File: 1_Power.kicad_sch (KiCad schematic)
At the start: 35 parts, among them Q201 IRLZ44N, Q202 IRLZ44N, U201 BQ24005, U202 LM74700, U203 LM74700, U204 NCP1117-3.3, U205 LMR51430, U206 TPS7A2033PDBVR

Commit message: Changed oscillator series resistors to DNP
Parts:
- D201, D202: footprint (none) -> LED_SMD:LED_0603_1608Metric
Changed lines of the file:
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@@
 			)
 		)
-		(property "Footprint" ""
+		(property "Footprint" "LED_SMD:LED_0603_1608Metric"
 			(at 88.9 119.38 0)
 			(hide yes)
@@
 			)
 		)
-		(property "Footprint" ""
+		(property "Footprint" "LED_SMD:LED_0603_1608Metric"
 			(at 95.25 116.84 0)
 			(hide yes)

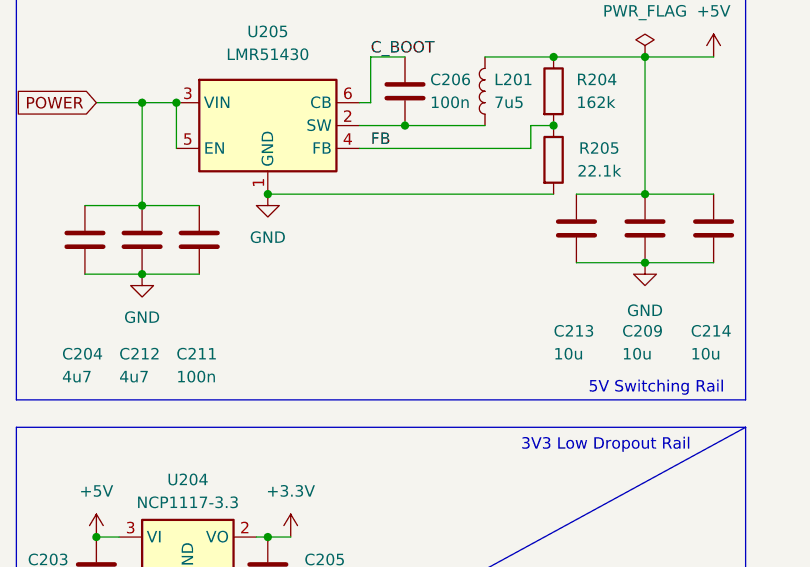
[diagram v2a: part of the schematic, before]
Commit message: Added switching regulator notes
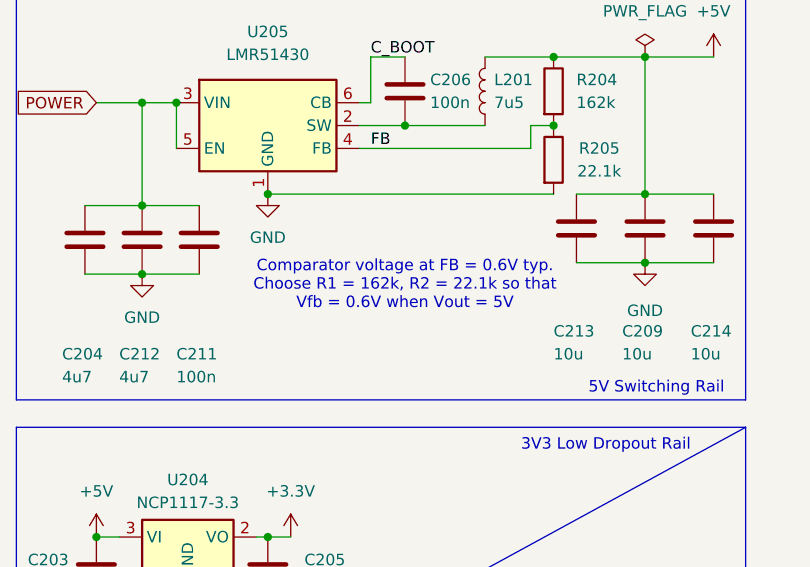
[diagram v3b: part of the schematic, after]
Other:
- note added: "Comparator voltage at FB = 0.6V typ. Choose R1 = 162k, R2 = 22.1k so that Vfb = 0.6V when Vout = 5V"
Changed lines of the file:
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@@
+		)
+	)
+	(text "Comparator voltage at FB = 0.6V typ.\nChoose R1 = 162k, R2 = 22.1k so that\nVfb = 0.6V when Vout = 5V"
+		(exclude_from_sim no)
+		(at 236.22 88.9 0)
+		(effects
+			(font
+				(size 1.27 1.27)
+			)
 		)
 	)

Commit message: Redid ESD protection because the previous chip couldn't handle 9V from USB-PD Finished status indication sections
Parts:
- D202: value RED -> ORANGE
- R206, R207: value 330R -> 180R
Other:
- note added: "Output inductor calculations: Lmin = (Vin_max - Vout) * Vout / Iout * K * Vin_max * f Vin_max = 9V, Vout = 5V, Iout = 2A, K = 0.3, f = 500kHz Lmin = ~7.4 uH = 7.5 uH standard value -------------------------------------------- Output capacitor calculations: ΔVout_esr = K * Iout * ESR = 30 mV max ⇒ ESR = 0.05 Ω max ΔVout_c = K * Iout / 8 * f * Cout = 30 mV max ⇒ Cout = 5 uF Cout > 4 * (Ioh - Iol) /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"
- note removed: "Output inductor calculations: Lmin = (Vin_max - Vout) * Vout / Iout * K * Vin_max * f Vin_max = 9V, Vout = 5V, Iout = 2A, K = 0.3, f = 500kHz Lmin = ~7.4 uH = 7.5 uH standard value -------------------------------------------------------- Output capacitor calculations: ΔVout_esr = K * Iout * ESR = 30 mV max ⇒ ESR = 0.05 Ω max ΔVout_c = K * Iout / 8 * f * Cout = 30 mV max ⇒ Cout = 5 uF Cout > 4 * (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"
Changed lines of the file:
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@@
 		)
 	)
-	(text "Output inductor calculations:\nLmin = (Vin_max - Vout) * Vout / Iout * K * Vin_max * f\nVin_max = 9V, Vout = 5V, Iout = 2A, K = 0.3, f = 500kHz\nLmin = ~7.4 uH = 7.5 uH standard value\n--------------------------------------------------------\nOutput capacitor calculations:\nΔVout_esr = K * Iout * ESR = 30 mV max\n⇒ ESR = 0.05 Ω max\n\nΔVout_c = K * Iout / 8 * f * Cout = 30 mV max\n⇒ Cout = 5 uF\n\nCout > 4 * (Ioh - Iol) / f * ΔVout_shoot\nUsing Ioh = 1.5A, Iol = 0.5A, ΔVout_shoot = 250 mV:\nCout > 32 uF\nUsing Cout > 32 uF at 50 mΩ ESR: \nChoose Cout = 3 x 10 uF at 25V (CL31B106KAHNNWE from Samsung)"
+	(text "Output inductor calculations:\nLmin = (Vin_max - Vout) * Vout / Iout * K * Vin_max * f\nVin_max = 9V, Vout = 5V, Iout = 2A, K = 0.3, f = 500kHz\nLmin = ~7.4 uH = 7.5 uH standard value\n--------------------------------------------\nOutput capacitor calculations:\nΔVout_esr = K * Iout * ESR = 30 mV max\n⇒ ESR = 0.05 Ω max\n\nΔVout_c = K * Iout / 8 * f * Cout = 30 mV max\n⇒ Cout = 5 uF\n\nCout > 4 * (Ioh - Iol) / f * ΔVout_shoot\nUsing Ioh = 1.5A, Iol = 0.5A, ΔVout_shoot = 250 mV:\nCout > 32 uF\nUsing Cout > 32 uF at 50 mΩ ESR: \nChoose Cout = 3 x 10 uF at 25V (CL31B106KAHNNWE from Samsung)"
 		(exclude_from_sim no)
 		(at 193.04 39.37 0)
@@
 			)
 		)
-		(property "Value" "330R"
+		(property "Value" "180R"
 			(at 96.52 125.73 0)
 			(show_name no)
@@
 			)
 		)
-		(property "Value" "330R"
+		(property "Value" "180R"
 			(at 81.28 128.27 0)
 			(show_name no)
@@
 			)
 		)
-		(property "Value" "RED"
+		(property "Value" "ORANGE"
 			(at 96.52 118.11 90)
 			(show_name no)
